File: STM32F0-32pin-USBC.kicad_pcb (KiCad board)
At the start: 2 copper layers, 45.6 x 38.8 mm, 30 parts, among them J1 Conn_ARM_JTAG_SWD_10, J2 USB_C_Receptacle_USB2.0_16P, J3 Conn_01x12, U1 STM32F042K6Tx, U2 USBLC6-2SC6, U3 MCP1755S, U4 MCP2221AxSL

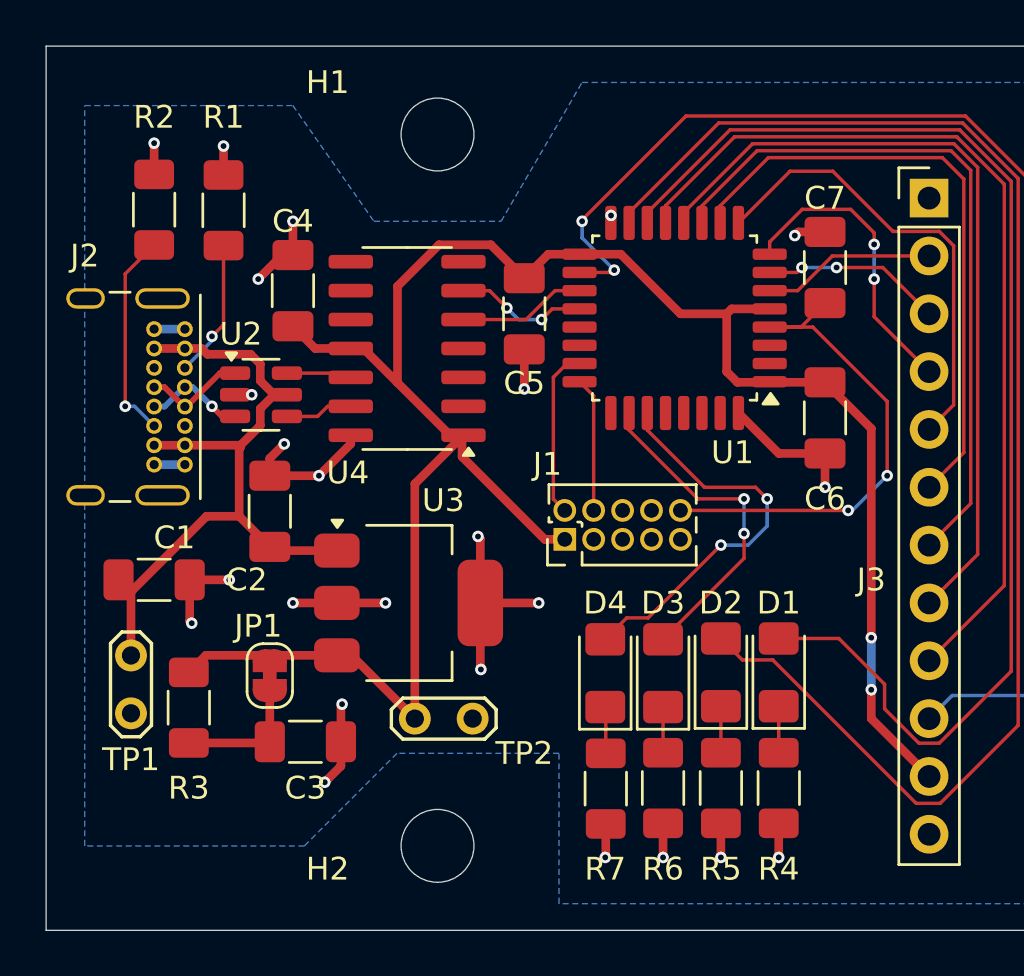
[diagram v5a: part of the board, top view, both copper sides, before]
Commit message: update all R's and all C's but 10u to 0805 from 1206
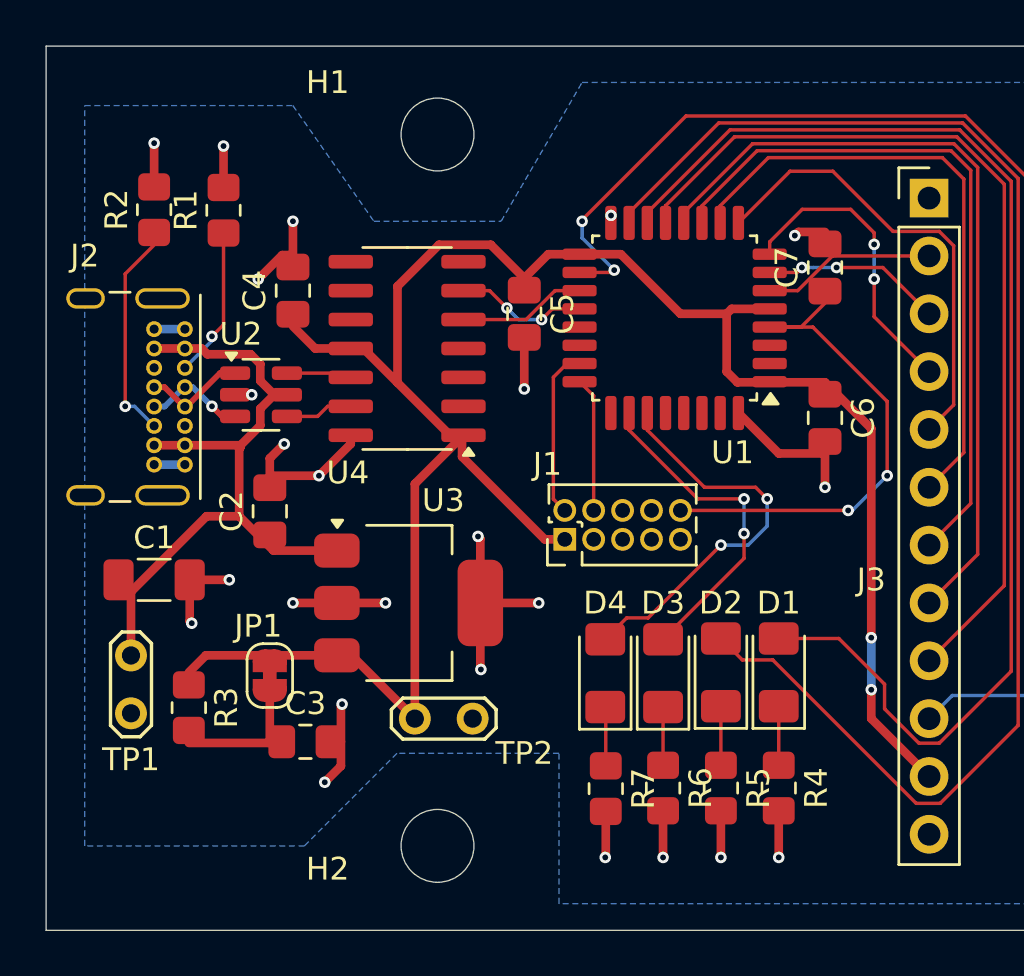
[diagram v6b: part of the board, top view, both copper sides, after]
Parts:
- C2, C3, C4, C5, C6, C7: footprint Capacitor_SMD:C_1206_3216Metric_Pad1.33x1.80mm_HandSolder -> Capacitor_SMD:C_0805_2012Metric_Pad1.18x1.45mm_HandSolder
- R1, R2, R3, R4, R5, R6, R7: footprint Resistor_SMD:R_1206_3216Metric_Pad1.30x1.75mm_HandSolder -> Resistor_SMD:R_0805_2012Metric_Pad1.20x1.40mm_HandSolder

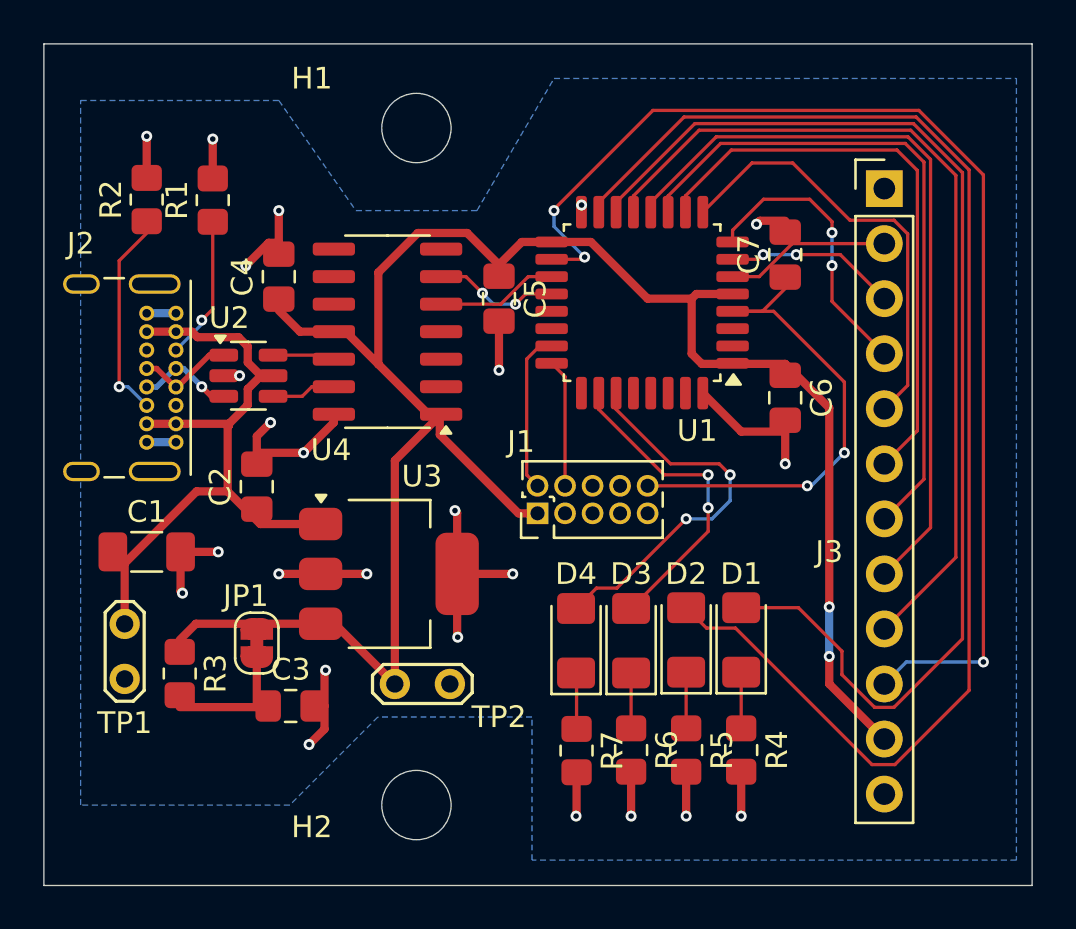
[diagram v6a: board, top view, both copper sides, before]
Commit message: Changed to 0805 for most Rs and C's
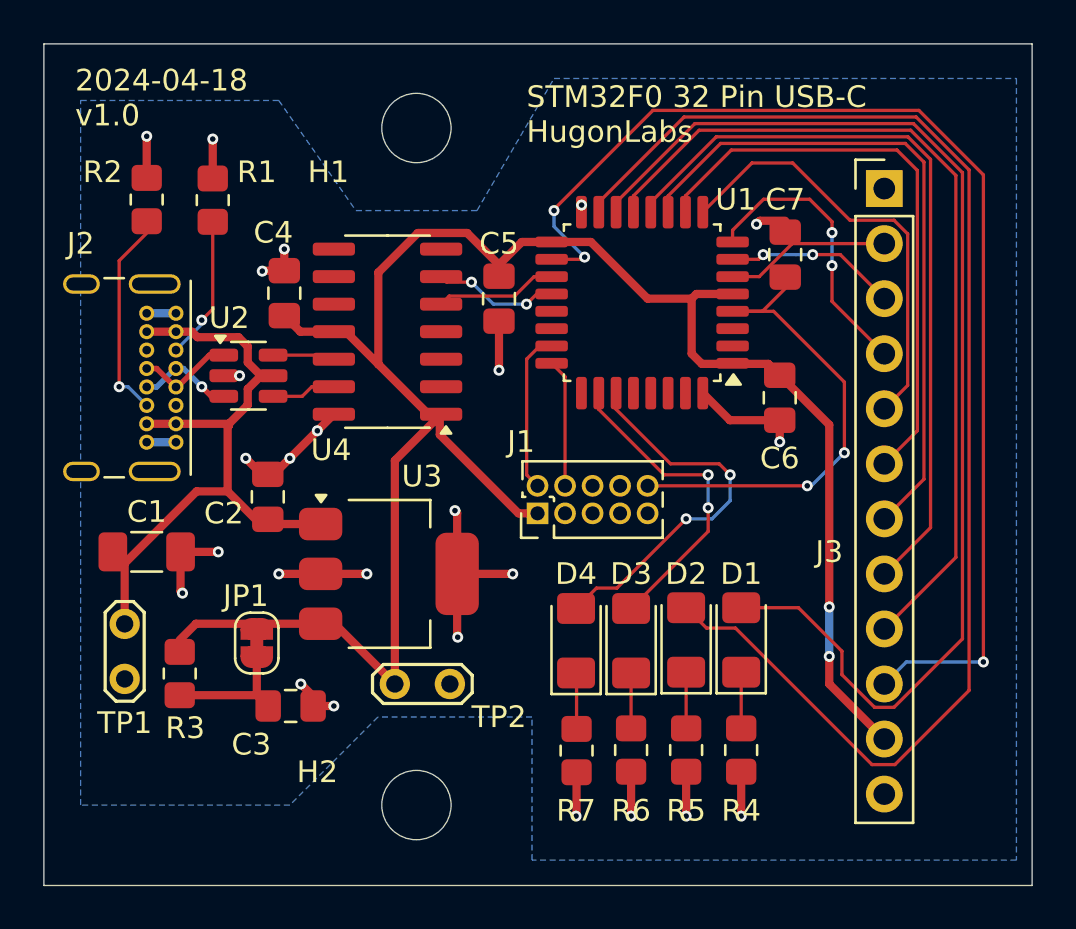
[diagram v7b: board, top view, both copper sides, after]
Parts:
- moved C4 0.80 mm to (91.7, 80.0)
- moved C2 0.69 mm to (90.9, 89.4)
- moved C6 0.25 mm to (114.6, 84.8)
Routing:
- net GND: track 51.1 -> 46.5 mm, vias 24 -> 25
- net /USB_and_LDO/ldo_jumper: track 5.83 -> 6.76 mm
- net +3.3V: track 91.0 -> 90.2 mm
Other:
- board text added: "2024-04-18 v1.0"
- board text added: "STM32F0 32 Pin USB-C HugonLabs"

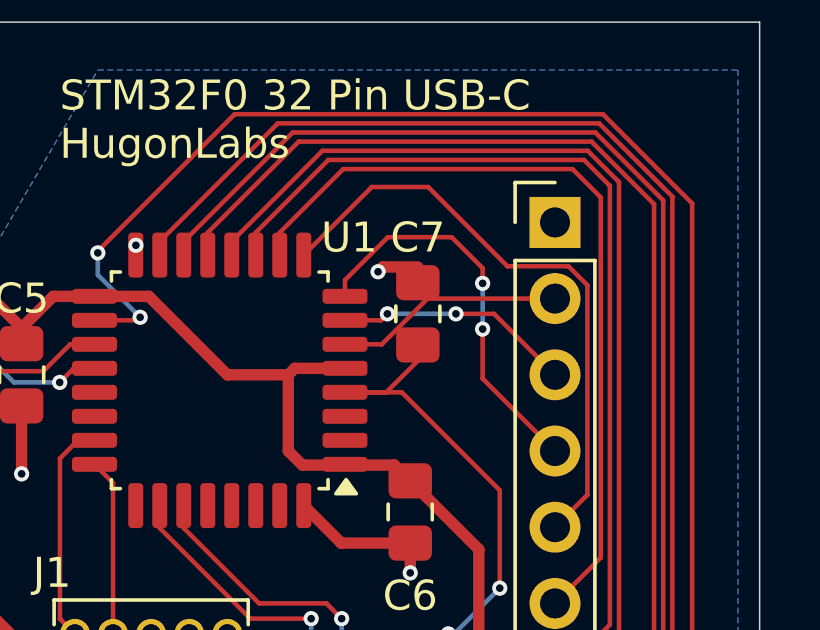
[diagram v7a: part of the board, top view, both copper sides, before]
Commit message: fixed DRC violations
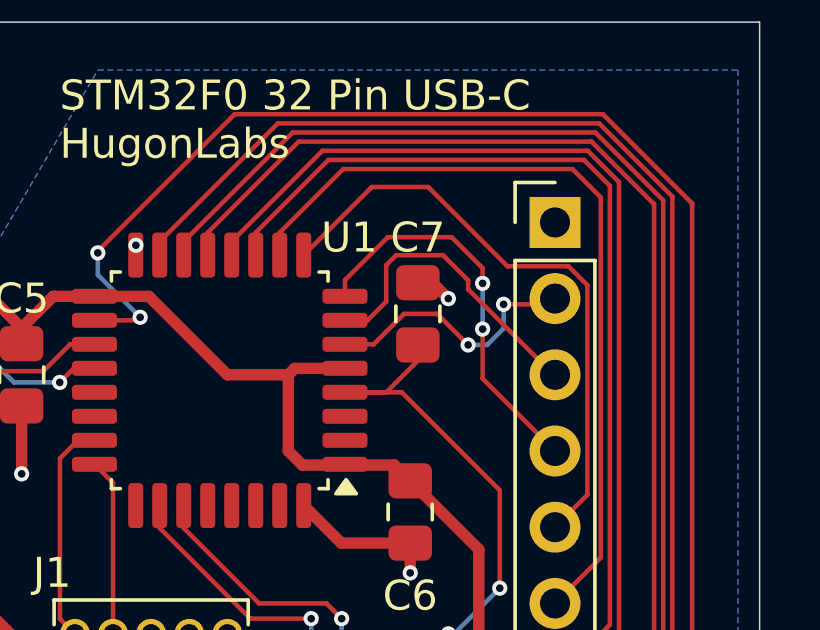
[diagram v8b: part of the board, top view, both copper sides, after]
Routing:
- net /PA1: track 7.93 -> 10.4 mm, vias 2 -> 0
- net /PA0: track 7.63 -> 8.96 mm, vias 0 -> 2
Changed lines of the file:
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@@
+	)
+	(segment
+		(start 114.808 77.1945)
+		(end 115.2945 77.1945)
+		(width 0.381)
+		(layer "F.Cu")
+		(net 2)
 	)
 	(segment
@@
 	)
 	(segment
-		(start 114.808 76.6695)
-		(end 113.640684 76.6695)
-		(width 0.381)
-		(layer "F.Cu")
-		(net 2)
-	)
-	(segment
 		(start 88.9 83.82)
 		(end 89.629764 83.82)
@@
 	)
 	(segment
-		(start 113.640684 76.6695)
-		(end 113.481192 76.828992)
-		(width 0.381)
-		(layer "F.Cu")
-		(net 2)
-	)
-	(segment
 		(start 85.344 74.142)
 		(end 85.344 72.771)
@@
 	)
 	(segment
+		(start 115.2945 77.1945)
+		(end 115.824 77.724)
+		(width 0.381)
+		(layer "F.Cu")
+		(net 2)
+	)
+	(segment
 		(start 112.776 102.642)
 		(end 112.776 104.14)
@@
 	)
 	(via
-		(at 113.481192 76.828992)
-		(size 0.508)
-		(drill 0.254)
-		(layers "F.Cu" "B.Cu")
-		(net 2)
-	)
-	(via
 		(at 92.456 98.044)
 		(size 0.508)
@@
 	(via
 		(at 93.98 99.06)
+		(size 0.508)
+		(drill 0.254)
+		(layers "F.Cu" "B.Cu")
+		(net 2)
+	)
+	(via
+		(at 115.824 77.724)
 		(size 0.508)
 		(drill 0.254)
@@
 	)
 	(segment
+		(start 119.1895 77.9145)
+		(end 119.38 77.724)
+		(width 0.1524)
+		(layer "F.Cu")
+		(net 25)
+	)
+	(segment
 		(start 112.379 79.248)
-		(end 113.60823 79.248)
+		(end 113.33323 79.248)
 		(width 0.1524)
 		(layer "F.Cu")
@@
 	)
 	(segment
-		(start 113.60823 79.248)
-		(end 115.13223 77.724)
+		(start 115.448078 78.232)
+		(end 116.4844 79.268322)
 		(width 0.1524)
 		(layer "F.Cu")
@@
 	)
 	(segment
-		(start 115.13223 77.724)
-		(end 119.38 77.724)
-		(width 0.1524)
-		(layer "F.Cu")
+		(start 114.34923 78.232)
+		(end 115.448078 78.232)
+		(width 0.1524)
+		(layer "F.Cu")
+		(net 25)
+	)
+	(segment
+		(start 117.6655 77.9145)
+		(end 119.1895 77.9145)
+		(width 0.1524)
+		(layer "F.Cu")
+		(net 25)
+	)
+	(segment
+		(start 113.33323 79.248)
+		(end 114.34923 78.232)
+		(width 0.1524)
+		(layer "F.Cu")
+		(net 25)
+	)
+	(via
+		(at 117.6655 77.9145)
+		(size 0.508)
+		(drill 0.254)
+		(layers "F.Cu" "B.Cu")
+		(net 25)
+	)
+	(via
+		(at 116.4844 79.268322)
+		(size 0.508)
+		(drill 0.254)
+		(layers "F.Cu" "B.Cu")
+		(net 25)
+	)
+	(segment
+		(start 117.6655 78.724)
+		(end 117.6655 77.9145)
+		(width 0.1524)
+		(layer "B.Cu")
+		(net 25)
+	)
+	(segment
+		(start 117.121178 79.268322)
+		(end 117.6655 78.724)
+		(width 0.1524)
+		(layer "B.Cu")
+		(net 25)
+	)
+	(segment
+		(start 116.4844 79.268322)
+		(end 117.121178 79.268322)
+		(width 0.1524)
+		(layer "B.Cu")
 		(net 25)
 	)
@@
 	)
 	(segment
-		(start 116.078 78.232)
-		(end 117.348 78.232)
+		(start 113.128999 78.448)
+		(end 113.7528 77.824199)
 		(width 0.1524)
 		(layer "F.Cu")
@@
 	)
 	(segment
-		(start 117.348 78.232)
+		(start 113.7528 76.609746)
+		(end 114.085746 76.2768)
+		(width 0.1524)
+		(layer "F.Cu")
+		(net 32)
+	)
+	(segment
+		(start 112.379 78.448)
+		(end 113.128999 78.448)
+		(width 0.1524)
+		(layer "F.Cu")
+		(net 32)
+	)
+	(segment
+		(start 115.6468 76.2768)
+		(end 116.4844 77.1144)
+		(width 0.1524)
+		(layer "F.Cu")
+		(net 32)
+	)
+	(segment
+		(start 114.085746 76.2768)
+		(end 115.6468 76.2768)
+		(width 0.1524)
+		(layer "F.Cu")
+		(net 32)
+	)
+	(segment
+		(start 113.7528 77.824199)
+		(end 113.7528 76.609746)
+		(width 0.1524)
+		(layer "F.Cu")
+		(net 32)
+	)
+	(segment
+		(start 116.4844 77.4159)
+		(end 119.3325 80.264)
+		(width 0.1524)
+		(layer "F.Cu")
+		(net 32)
+	)
+	(segment
+		(start 119.3325 80.264)
 		(end 119.38 80.264)
 		(width 0.1524)
@@
 	)
 	(segment
-		(start 112.379 78.448)
-		(end 113.576 78.448)
+		(start 116.4844 77.1144)
+		(end 116.4844 77.4159)
 		(width 0.1524)
 		(layer "F.Cu")
 		(net 32)
 	)
-	(segment
-		(start 113.576 78.448)
-		(end 113.792 78.232)
-		(width 0.1524)
-		(layer "F.Cu")
-		(net 32)
-	)
-	(via
-		(at 116.078 78.232)
-		(size 0.508)
-		(drill 0.254)
-		(layers "F.Cu" "B.Cu")
-		(net 32)
-	)
-	(via
-		(at 113.792 78.232)
-		(size 0.508)
-		(drill 0.254)
-		(layers "F.Cu" "B.Cu")
-		(net 32)
-	)
-	(segment
-		(start 115.316 78.232)
-		(end 113.792 78.232)
-		(width 0.1524)
-		(layer "B.Cu")
-		(net 32)
-	)
-	(segment
-		(start 116.078 78.232)
-		(end 115.316 78.232)
-		(width 0.1524)
-		(layer "B.Cu")
-		(net 32)
-	)
